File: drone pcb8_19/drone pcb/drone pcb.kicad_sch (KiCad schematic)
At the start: 9 parts, among them J1 Conn_01x03_Socket, J2 Conn_01x03_Socket, J3 Conn_01x03_Socket, J4 Conn_01x03_Socket, U1 MS560702BA03-50

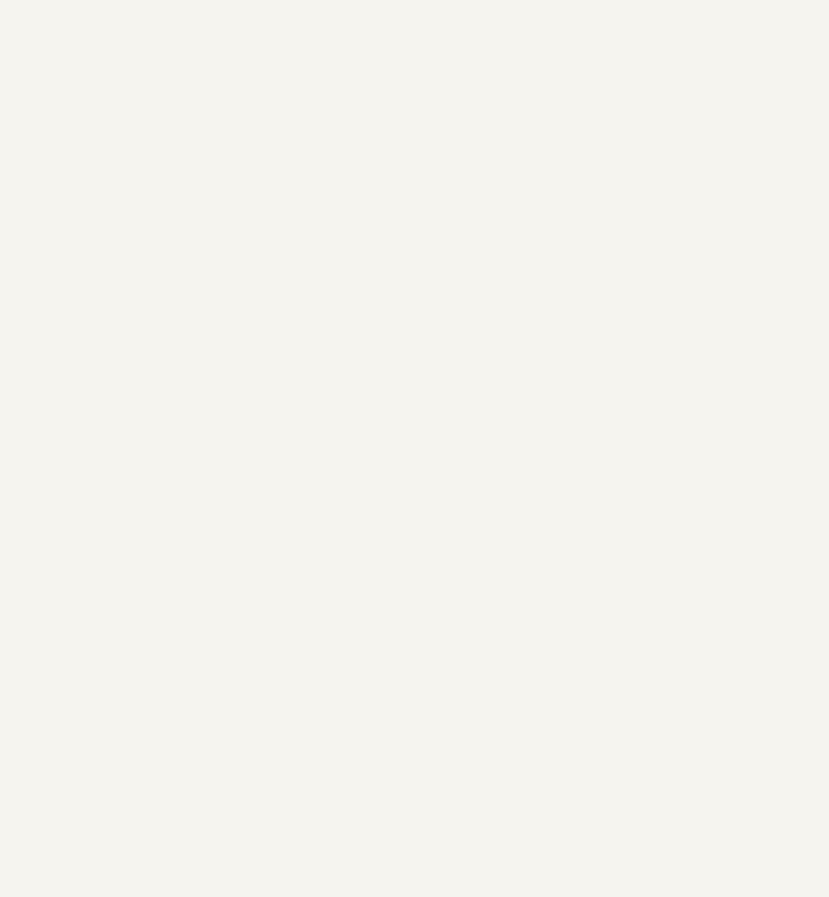
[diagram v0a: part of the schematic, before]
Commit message: add feather power off battery
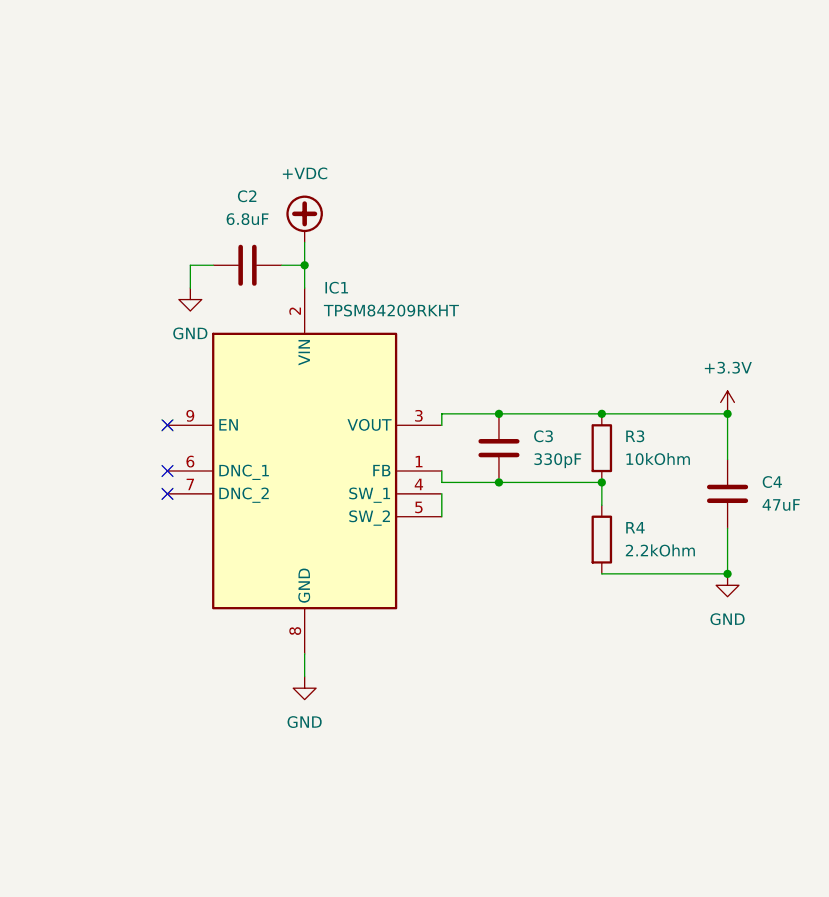
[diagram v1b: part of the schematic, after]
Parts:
- added C2: 6.8uF, Capacitor_SMD:C_0603_1608Metric_Pad1.08x0.95mm_HandSolder, symbol Device:C
- added C3: 330pF, Capacitor_SMD:C_0603_1608Metric_Pad1.08x0.95mm_HandSolder, symbol Device:C
- added C4: 47uF, Capacitor_SMD:C_0603_1608Metric_Pad1.08x0.95mm_HandSolder, symbol Device:C
- added IC1: TPSM84209RKHT, TPSM84209RKHT, symbol TPSM84209RKHT:TPSM84209RKHT
- added R3: 10kOhm, Resistor_SMD:R_0603_1608Metric_Pad0.98x0.95mm_HandSolder, symbol Device:R
- added R4: 2.2kOhm, Resistor_SMD:R_0603_1608Metric_Pad0.98x0.95mm_HandSolder, symbol Device:R
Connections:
- net +3.3V: now also C3.1, C4.1, IC1.3 (VOUT), R3.1
- net GND: now also C2.1, C4.2, IC1.8 (GND), R4.2
- new net: C3.2, IC1.1 (FB), R3.2, R4.1
- new net: IC1.4 (SW_1), IC1.5 (SW_2)
- new net +VDC: C2.2, IC1.2 (VIN)
- no-connect marks 1 -> 4
